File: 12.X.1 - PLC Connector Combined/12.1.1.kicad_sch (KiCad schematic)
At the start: 30 parts, among them J201 Conn_01x01_PAD, J202 Conn_01x01_PAD, J203 Conn_01x01_PAD, J204 Conn_01x01_PAD, J205 Conn_01x01_PAD, J206 Conn_01x01_PAD, J207 Conn_01x01_PAD, J208 Conn_01x01_PAD, J209 Conn_01x01_PAD, J210 Conn_01x01_PAD, J211 Conn_01x01_PAD, J212 Conn_01x01_PAD, J213 Conn_01x01_PAD, J214 Conn_01x01_PAD, J215 Conn_01x01_PAD, J216 Conn_01x01_PAD, J217 Conn_01x01_PAD, J218 Conn_01x01_PAD, J219 Conn_01x01_PAD, J220 Conn_01x01_PAD, J221 DB128L-5.08-2P-BK-S, J222 DB128L-5.08-2P-BK-S, J223 DB128L-5.08-2P-BK-S, J224 DB128L-5.08-2P-BK-S, J225 DB128L-5.08-2P-BK-S, J226 B04B-XASK-1

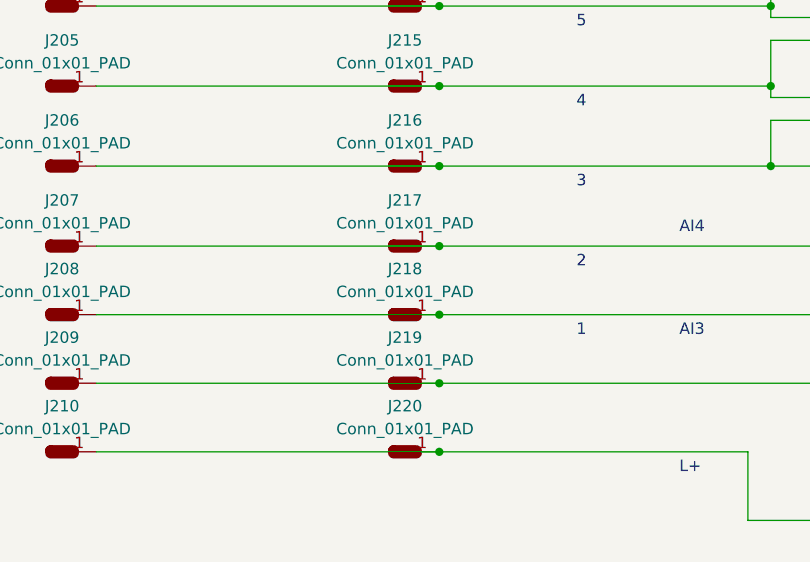
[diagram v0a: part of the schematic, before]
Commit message: worked on layout, added V-Cut lines
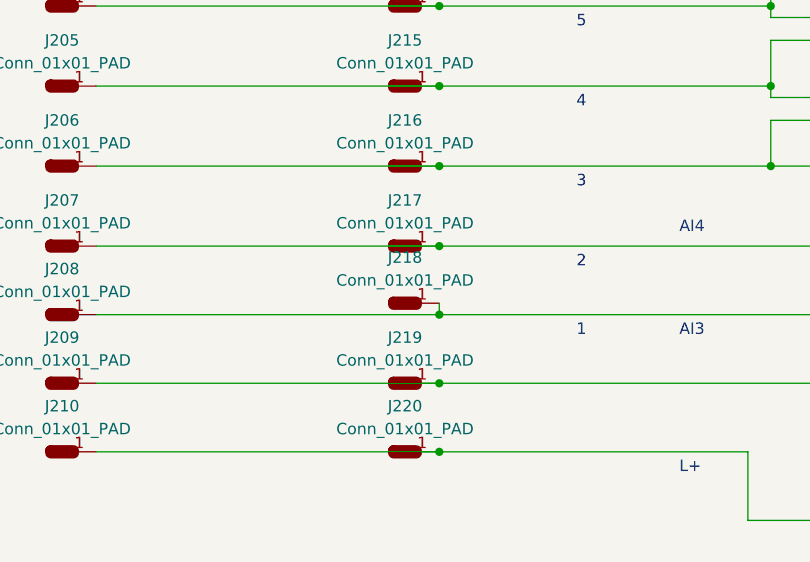
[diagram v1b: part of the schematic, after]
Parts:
- J201, J202, J203, J204, J205, J206, J207, J208, J209, J210, J211, J212, J213, J214, J215, J216, J217, J218, J219, J220: footprint PCB_FOOTPRINT_Library:Conn_pin_PLC -> PCB_Library:Conn_pin_PLC
- J221, J222, J223, J224, J225: footprint 1729128 -> PCB_Library:1729128
- J226: footprint PCB_FOOTPRINT_Library:CONN_B04B-XASK-1_JST -> PCB_Library:CONN_B04B-XASK-1_JST
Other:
- moved on the sheet: J218
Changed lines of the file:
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@@
+    (stroke (width 0) (type default))
+  )
+  (wire (pts (xy 101.6 119.38) (xy 101.6 120.65))
     (stroke (width 0) (type default))
   )
@@
       (effects (font (size 1.27 1.27)))
     )
-    (property "Footprint" "PCB_FOOTPRINT_Library:Conn_pin_PLC" (at 96.52 68.58 0)
+    (property "Footprint" "PCB_Library:Conn_pin_PLC" (at 96.52 68.58 0)
       (effects (font (size 1.27 1.27)) hide)
     )
@@
       (effects (font (size 1.27 1.27)))
     )
-    (property "Footprint" "PCB_FOOTPRINT_Library:Conn_pin_PLC" (at 96.52 135.89 0)
+    (property "Footprint" "PCB_Library:Conn_pin_PLC" (at 96.52 135.89 0)
       (effects (font (size 1.27 1.27)) hide)
     )
@@
       (effects (font (size 1.27 1.27)))
     )
-    (property "Footprint" "PCB_FOOTPRINT_Library:Conn_pin_PLC" (at 58.42 68.58 0)
+    (property "Footprint" "PCB_Library:Conn_pin_PLC" (at 58.42 68.58 0)
       (effects (font (size 1.27 1.27)) hide)
     )
@@
       (effects (font (size 1.27 1.27)) (justify left))
     )
-    (property "Footprint" "1729128" (at 163.83 77.47 0)
+    (property "Footprint" "PCB_Library:1729128" (at 163.83 77.47 0)
       (effects (font (size 1.27 1.27)) (justify left) hide)
     )
@@
       (effects (font (size 1.27 1.27)))
     )
-    (property "Footprint" "PCB_FOOTPRINT_Library:Conn_pin_PLC" (at 96.52 128.27 0)
+    (property "Footprint" "PCB_Library:Conn_pin_PLC" (at 96.52 128.27 0)
       (effects (font (size 1.27 1.27)) hide)
     )
@@
       (effects (font (size 1.27 1.27)))
     )
-    (property "Footprint" "PCB_FOOTPRINT_Library:Conn_pin_PLC" (at 96.52 95.25 0)
+    (property "Footprint" "PCB_Library:Conn_pin_PLC" (at 96.52 95.25 0)
       (effects (font (size 1.27 1.27)) hide)
     )
@@
       (effects (font (size 1.27 1.27)))
     )
-    (property "Footprint" "PCB_FOOTPRINT_Library:Conn_pin_PLC" (at 58.42 120.65 0)
+    (property "Footprint" "PCB_Library:Conn_pin_PLC" (at 58.42 120.65 0)
       (effects (font (size 1.27 1.27)) hide)
     )
@@
     )
   )
-  (symbol (lib_id "PCB_Library:Conn_01x01_PAD") (at 96.52 120.65 0) (unit 1)
-    (in_bom yes) (on_board yes) (dnp no) (fields_autoplaced)
-    (property "Reference" "J218" (at 97.79 115.57 0)
-      (effects (font (size 1.27 1.27)))
-    )
-    (property "Value" "Conn_01x01_PAD" (at 97.79 118.11 0)
-      (effects (font (size 1.27 1.27)))
-    )
-    (property "Footprint" "PCB_FOOTPRINT_Library:Conn_pin_PLC" (at 96.52 120.65 0)
-      (effects (font (size 1.27 1.27)) hide)
-    )
-    (property "Datasheet" "~" (at 96.52 120.65 0)
+  (symbol (lib_id "PCB_Library:Conn_01x01_PAD") (at 96.52 119.38 0) (unit 1)
+    (in_bom yes) (on_board yes) (dnp no) (fields_autoplaced)
+    (property "Reference" "J218" (at 97.79 114.3 0)
+      (effects (font (size 1.27 1.27)))
+    )
+    (property "Value" "Conn_01x01_PAD" (at 97.79 116.84 0)
+      (effects (font (size 1.27 1.27)))
+    )
+    (property "Footprint" "PCB_Library:Conn_pin_PLC" (at 96.52 119.38 0)
+      (effects (font (size 1.27 1.27)) hide)
+    )
+    (property "Datasheet" "~" (at 96.52 119.38 0)
       (effects (font (size 1.27 1.27)) hide)
     )
@@
       (effects (font (size 1.27 1.27)) (justify left))
     )
-    (property "Footprint" "1729128" (at 233.68 115.57 0)
+    (property "Footprint" "PCB_Library:1729128" (at 233.68 115.57 0)
       (effects (font (size 1.27 1.27)) (justify left) hide)
     )
@@
       (effects (font (size 1.27 1.27)))
     )
-    (property "Footprint" "PCB_FOOTPRINT_Library:Conn_pin_PLC" (at 96.52 77.47 0)
+    (property "Footprint" "PCB_Library:Conn_pin_PLC" (at 96.52 77.47 0)
       (effects (font (size 1.27 1.27)) hide)
     )
@@
       (effects (font (size 1.27 1.27)))
     )
-    (property "Footprint" "PCB_FOOTPRINT_Library:Conn_pin_PLC" (at 96.52 86.36 0)
+    (property "Footprint" "PCB_Library:Conn_pin_PLC" (at 96.52 86.36 0)
       (effects (font (size 1.27 1.27)) hide)
     )
@@
       (effects (font (size 1.27 1.27)) (justify left))
     )
-    (property "Footprint" "1729128" (at 165.1 138.43 0)
+    (property "Footprint" "PCB_Library:1729128" (at 165.1 138.43 0)
       (effects (font (size 1.27 1.27)) (justify left) hide)
     )
@@
       (effects (font (size 1.27 1.27)))
     )
-    (property "Footprint" "PCB_FOOTPRINT_Library:Conn_pin_PLC" (at 58.42 104.14 0)
+    (property "Footprint" "PCB_Library:Conn_pin_PLC" (at 58.42 104.14 0)
       (effects (font (size 1.27 1.27)) hide)
     )
@@
       (effects (font (size 1.27 1.27)))
     )
-    (property "Footprint" "PCB_FOOTPRINT_Library:Conn_pin_PLC" (at 58.42 60.96 0)
+    (property "Footprint" "PCB_Library:Conn_pin_PLC" (at 58.42 60.96 0)
       (effects (font (size 1.27 1.27)) hide)
     )
@@
       (effects (font (size 1.27 1.27)))
     )
-    (property "Footprint" "PCB_FOOTPRINT_Library:Conn_pin_PLC" (at 96.52 60.96 0)
+    (property "Footprint" "PCB_Library:Conn_pin_PLC" (at 96.52 60.96 0)
       (effects (font (size 1.27 1.27)) hide)
     )
@@
       (effects (font (size 1.27 1.27)))
     )
-    (property "Footprint" "PCB_FOOTPRINT_Library:Conn_pin_PLC" (at 58.42 95.25 0)
+    (property "Footprint" "PCB_Library:Conn_pin_PLC" (at 58.42 95.25 0)
       (effects (font (size 1.27 1.27)) hide)
     )
@@
       (effects (font (size 1.27 1.27)))
     )
-    (property "Footprint" "PCB_FOOTPRINT_Library:Conn_pin_PLC" (at 58.42 135.89 0)
+    (property "Footprint" "PCB_Library:Conn_pin_PLC" (at 58.42 135.89 0)
       (effects (font (size 1.27 1.27)) hide)
     )
@@
       (effects (font (size 1.27 1.27)))
     )
-    (property "Footprint" "PCB_FOOTPRINT_Library:Conn_pin_PLC" (at 58.42 77.47 0)
+    (property "Footprint" "PCB_Library:Conn_pin_PLC" (at 58.42 77.47 0)
       (effects (font (size 1.27 1.27)) hide)
     )
@@
       (effects (font (size 1.27 1.27)))
     )
-    (property "Footprint" "PCB_FOOTPRINT_Library:Conn_pin_PLC" (at 58.42 86.36 0)
+    (property "Footprint" "PCB_Library:Conn_pin_PLC" (at 58.42 86.36 0)
       (effects (font (size 1.27 1.27)) hide)
     )
@@
       (effects (font (size 1.27 1.27)))
     )
-    (property "Footprint" "PCB_FOOTPRINT_Library:Conn_pin_PLC" (at 96.52 113.03 0)
+    (property "Footprint" "PCB_Library:Conn_pin_PLC" (at 96.52 113.03 0)
       (effects (font (size 1.27 1.27)) hide)
     )
@@
       (effects (font (size 1.27 1.27)))
     )
-    (property "Footprint" "PCB_FOOTPRINT_Library:Conn_pin_PLC" (at 58.42 113.03 0)
+    (property "Footprint" "PCB_Library:Conn_pin_PLC" (at 58.42 113.03 0)
       (effects (font (size 1.27 1.27)) hide)
     )
@@
       (effects (font (size 1.27 1.27)))
     )
-    (property "Footprint" "PCB_FOOTPRINT_Library:Conn_pin_PLC" (at 96.52 104.14 0)
+    (property "Footprint" "PCB_Library:Conn_pin_PLC" (at 96.52 104.14 0)
       (effects (font (size 1.27 1.27)) hide)
     )
@@
       (effects (font (size 1.524 1.524)))
     )
-    (property "Footprint" "PCB_FOOTPRINT_Library:CONN_B04B-XASK-1_JST" (at 228.6 86.36 0)
+    (property "Footprint" "PCB_Library:CONN_B04B-XASK-1_JST" (at 228.6 86.36 0)
       (effects (font (size 1.27 1.27) italic) hide)
     )
@@
       (effects (font (size 1.27 1.27)) (justify left))
     )
-    (property "Footprint" "1729128" (at 165.1 93.98 0)
+    (property "Footprint" "PCB_Library:1729128" (at 165.1 93.98 0)
       (effects (font (size 1.27 1.27)) (justify left) hide)
     )
@@
       (effects (font (size 1.27 1.27)) (justify left))
     )
-    (property "Footprint" "1729128" (at 208.28 45.72 0)
+    (property "Footprint" "PCB_Library:1729128" (at 208.28 45.72 0)
       (effects (font (size 1.27 1.27)) (justify left) hide)
     )
@@
       (effects (font (size 1.27 1.27)))
     )
-    (property "Footprint" "PCB_FOOTPRINT_Library:Conn_pin_PLC" (at 58.42 128.27 0)
-      (effects (font (size 1.27 1.27)) hide)
-    )
+    (property "Footprint" "PCB_Library:Conn_pin_PLC" (at 58.42 128.27 0)
+      (effects (font (size 1.27 1.27)) hide)
+    )

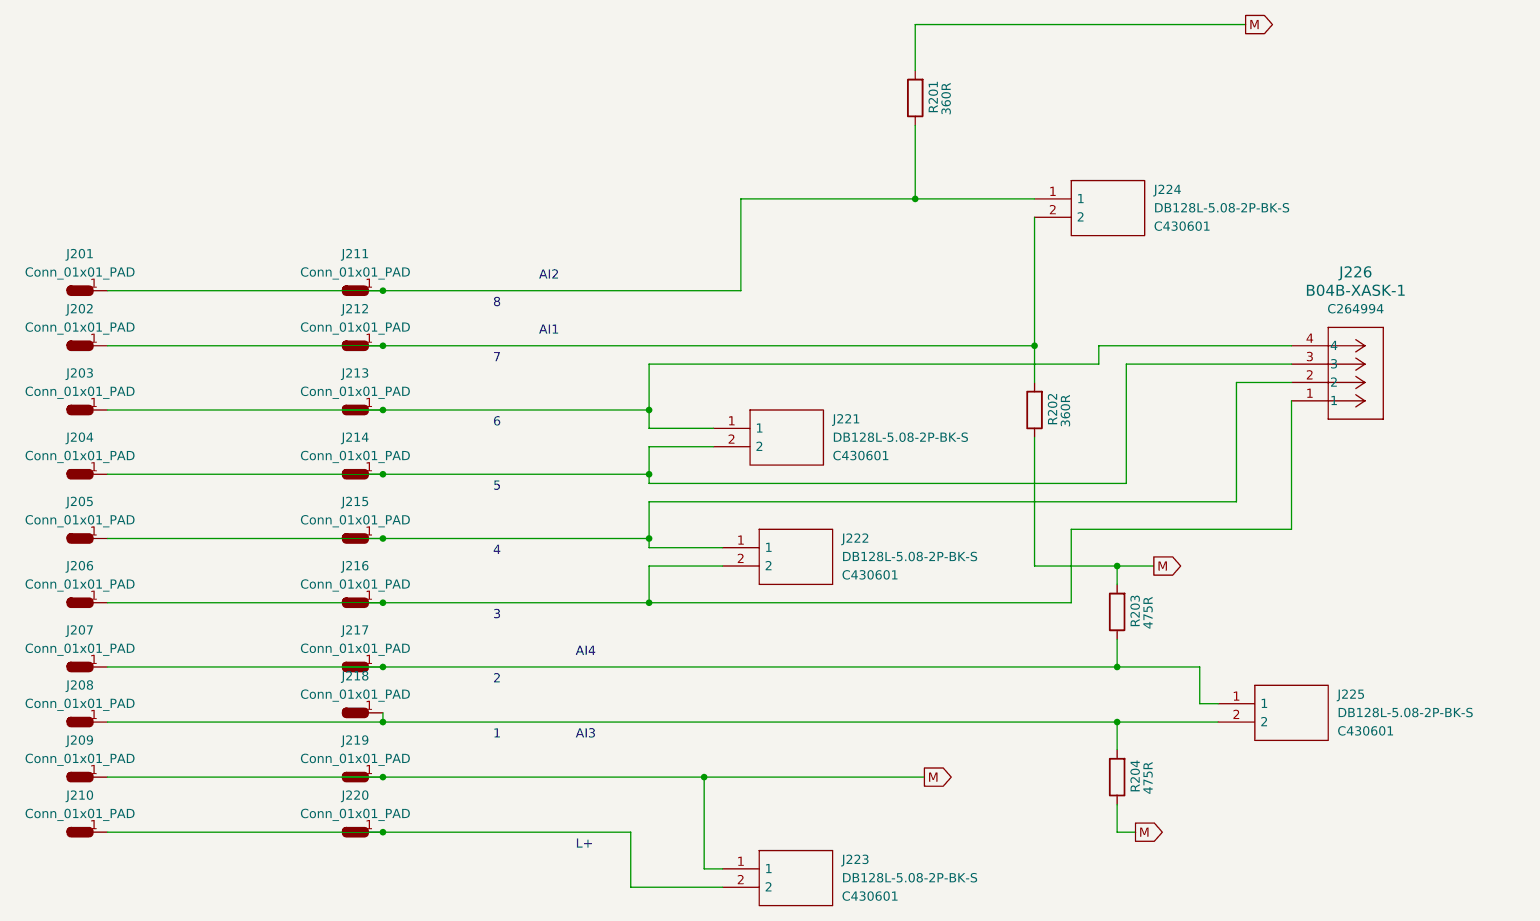
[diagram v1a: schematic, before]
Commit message: change pcb edge cuts
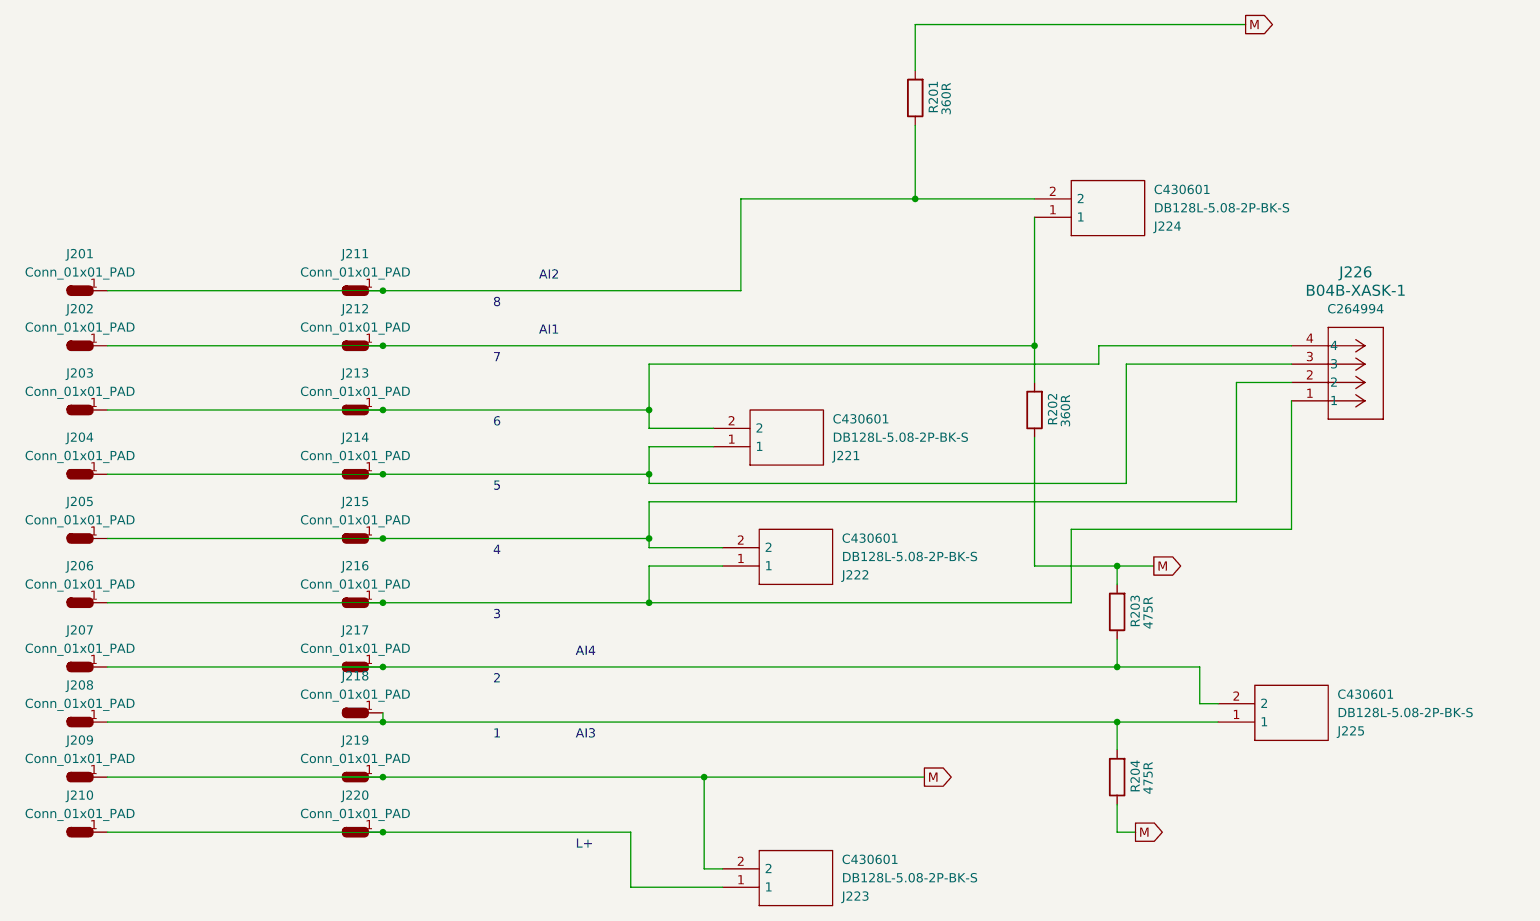
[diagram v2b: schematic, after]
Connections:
- net M: now also J223.2; no longer J223.1
- net at J202.1 (Pin_1), J212.1 (Pin_1), R202.2: now also J224.1; no longer J224.2
- net at J210.1 (Pin_1), J220.1 (Pin_1): now also J223.1; no longer J223.2
- net at J203.1 (Pin_1), J213.1 (Pin_1), J226.4: now also J221.2; no longer J221.1
- net at J204.1 (Pin_1), J214.1 (Pin_1), J226.3: now also J221.1; no longer J221.2
- net at J205.1 (Pin_1), J215.1 (Pin_1), J226.2: now also J222.2; no longer J222.1
- net at J208.1 (Pin_1), J218.1 (Pin_1), R204.2: now also J225.1; no longer J225.2
- net at J207.1 (Pin_1), J217.1 (Pin_1), R203.1: now also J225.2; no longer J225.1
- net at J201.1 (Pin_1), J211.1 (Pin_1), R201.1: now also J224.2; no longer J224.1
- net at J206.1 (Pin_1), J216.1 (Pin_1), J226.1: now also J222.1; no longer J222.2
